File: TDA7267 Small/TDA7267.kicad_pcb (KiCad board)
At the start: 2 copper layers, 43 x 39 mm, 18 parts, among them U1 TDA7267

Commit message: More stuff
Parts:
- D1: footprint LED_THT:LED_D5.0mm -> LED_THT:LED_D3.0mm
- moved OUT1 8.12 mm to (161.7, 88.6)
- moved H1 8.00 mm to (131.8, 89.5)
- moved H2 8.00 mm to (169.2, 89.5)
- moved C6 7.50 mm to (162.9, 96.9)
- moved C2 7.35 mm to (160.5, 106.6)
- moved D1 6.06 mm to (134.2, 94.3)
- moved R2 5.02 mm to (138.1, 89.9)
- moved TDA7267 4.66 mm to (149.6, 94.1)
- moved C5 3.96 mm to (140.9, 94.3)
- moved C3 2.38 mm to (140.6, 105.6)
- moved R1 2.38 mm to (145.6, 107.1)
- moved C1 2.31 mm to (155.5, 105.9)
- moved C4 0.90 mm to (135.5, 101.3)
- moved H3 0.54 mm to (131.8, 108.5)
- moved H4 0.54 mm to (169.2, 108.5)
- renumbered U1 to TDA7267
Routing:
- net Net-(OUT1-Pin_1): track 15.4 -> 11.8 mm
- net Net-(U1-SRV): track 17.7 -> 15.4 mm
- net Net-(C1-Pad1): track 13.1 -> 11.1 mm
- net Net-(U1-Out): track 17.3 -> 18.4 mm
- net Net-(D1-A): track 5.64 -> 4.94 mm
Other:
- board size 43 x 39 mm -> 43 x 31 mm
- board text removed: "TDA7267"

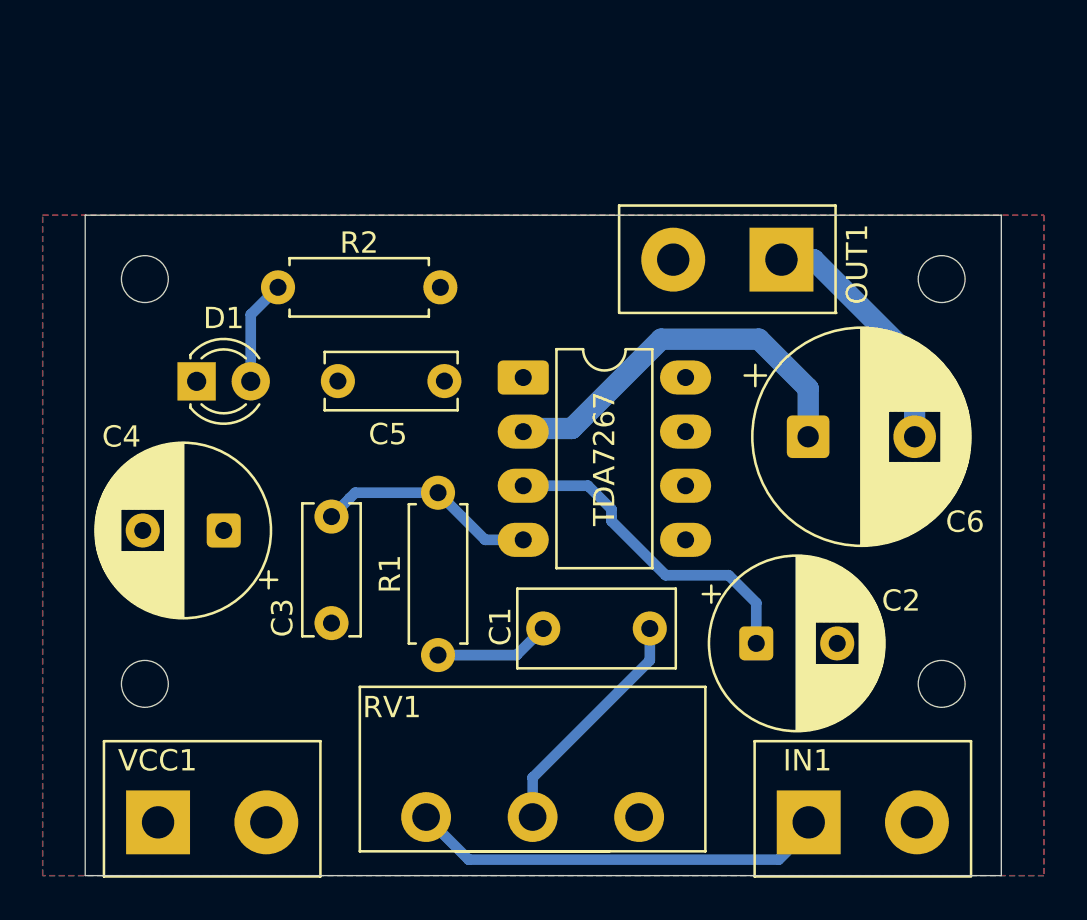
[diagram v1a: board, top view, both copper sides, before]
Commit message: Bottom GND plane
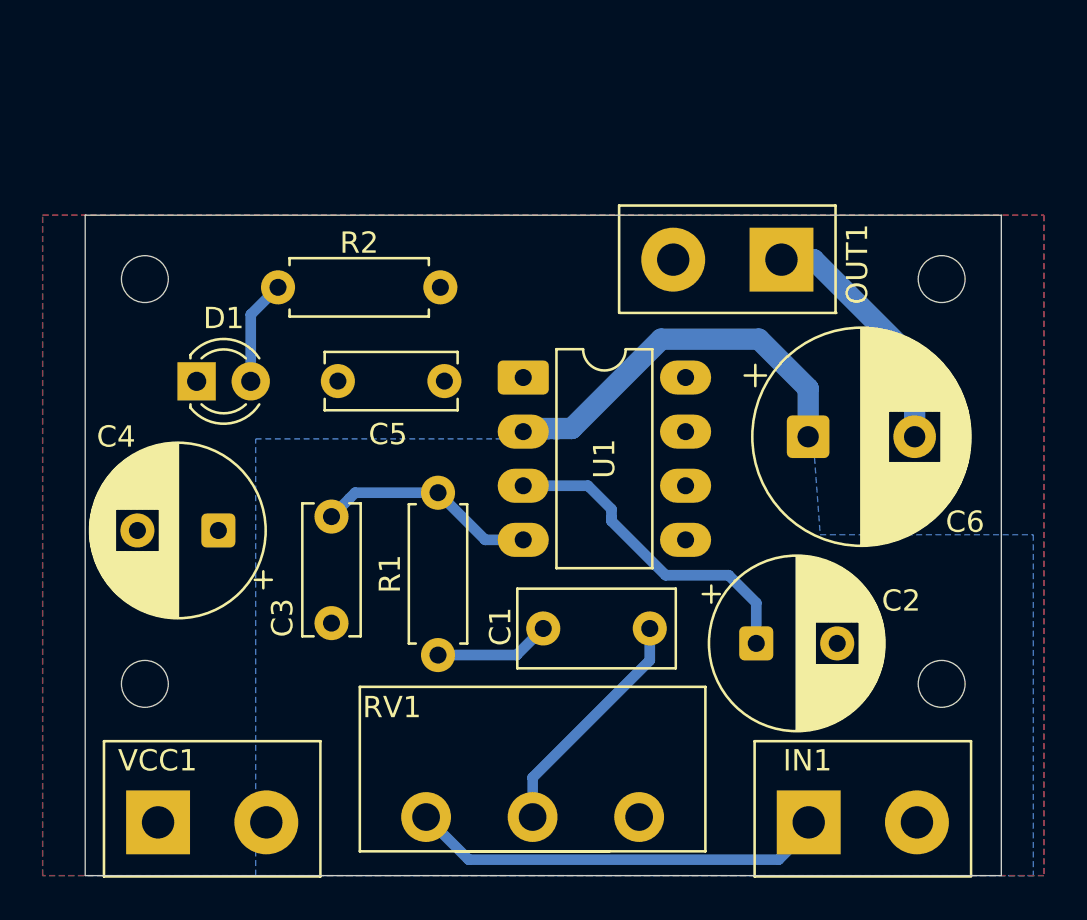
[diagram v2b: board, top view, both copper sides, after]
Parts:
- moved C4 0.25 mm to (135.2, 101.3)
- renumbered TDA7267 to U1
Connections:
- net Net-(U1-V+) renamed /VCC
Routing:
- added copper zone on B.Cu, net GND
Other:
- board text added: "TDA7267 2.5W Amplifier. 5 to 15V DC supply."
- board text removed: "TDA7267 2W Amplifier. 5 to 15V DC supply."
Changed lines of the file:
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@@
 	(net 4 "Net-(U1-SRV)")
 	(net 5 "Net-(U1-In)")
-	(net 6 "Net-(U1-V+)")
+	(net 6 "/VCC")
 	(net 7 "Net-(U1-Out)")
 	(net 8 "Net-(OUT1-Pin_1)")
@@
 			(layers "*.Cu" "*.Mask")
 			(remove_unused_layers no)
-			(net 6 "Net-(U1-V+)")
+			(net 6 "/VCC")
 			(pintype "passive")
 		)
@@
 		(descr "8-lead though-hole mounted DIP package, row spacing 7.62mm (300 mils), LongPads")
 		(tags "THT DIP DIL PDIP 2.54mm 7.62mm 300mil LongPads")
-		(property "Reference" "TDA7267"
+		(property "Reference" "U1"
 			(at 3.81 3.81 90)
 			(layer "F.SilkS")
@@
 			(remove_unused_layers no)
 			(roundrect_rratio 0.15625)
-			(net 6 "Net-(U1-V+)")
+			(net 6 "/VCC")
 			(pinfunction "V+")
 			(pintype "power_in")
@@
 			(layers "*.Cu" "*.Mask")
 			(remove_unused_layers no)
-			(net 6 "Net-(U1-V+)")
+			(net 6 "/VCC")
 			(pintype "passive")
 		)
@@
 			(layers "*.Cu" "*.Mask")
 			(remove_unused_layers no)
-			(net 6 "Net-(U1-V+)")
+			(net 6 "/VCC")
 			(pinfunction "Pin_1")
 			(pintype "passive")
@@
 	(footprint "Capacitor_THT:CP_Radial_D8.0mm_P3.80mm"
 		(layer "F.Cu")
-		(at 135.5 101.3 180)
+		(at 135.25 101.3 180)
 		(descr "CP, Radial series, Radial, pin pitch=3.80mm, diameter=8mm, height=14mm, Electrolytic Capacitor")
 		(tags "CP Radial series Radial pin pitch 3.80mm diameter 8mm height 14mm Electrolytic Capacitor")
@@
 			(remove_unused_layers no)
 			(roundrect_rratio 0.15625)
-			(net 6 "Net-(U1-V+)")
+			(net 6 "/VCC")
 			(pintype "passive")
 		)
@@
 		(layer "Edge.Cuts")
 	)
-	(gr_text "TDA7267 2W Amplifier.\n5 to 15V DC supply."
-		(at 162.4 112.6 0)
+	(gr_text "TDA7267 2.5W Amplifier.\n5 to 15V DC supply."
+		(at 164 112.6 0)
 		(layer "B.SilkS")
 		(effects
@@
 	)
 	(zone
-		(net 6)
-		(net_name "Net-(U1-V+)")
+		(net 3)
+		(net_name "GND")
 		(layer "B.Cu")
 		(hatch edge 0.5)
+		(priority 1)
 		(connect_pads yes
 			(clearance 0.5)
@@
 		(fill yes
 			(thermal_gap 0.5)
-			(thermal_bridge_width 10)
+			(thermal_bridge_width 0.5)
 		)
 		(polygon
 			(pts
-				(xy 127 86.5) (xy 174 86.5) (xy 174 117.5) (xy 127 117.5)
+				(xy 137 117.5) (xy 137 97) (xy 151.25 97) (xy 156.25 92.25) (xy 160.75 92.25) (xy 163 94.75) (xy 163.5 101.5)
+				(xy 173.5 101.5) (xy 173.5 117.5)
 			)
 		)
 	)
 	(zone
-		(net 0)
-		(net_name "")
+		(net 6)
+		(net_name "/VCC")
 		(layer "B.Cu")
 		(hatch edge 0.5)
-		(connect_pads
-			(clearance 0)
+		(connect_pads yes
+			(clearance 0.5)
 		)
 		(min_thickness 0.25)
 		(filled_areas_thickness no)
-		(keepout
-			(tracks allowed)
-			(vias allowed)
-			(pads allowed)
-			(copperpour not_allowed)
-			(footprints allowed)
-		)
-		(placement
-			(enabled no)
-			(sheetname "/")
-		)
-		(fill
+		(fill yes
 			(thermal_gap 0.5)
-			(thermal_bridge_width 0.5)
+			(thermal_bridge_width 10)
 		)
 		(polygon
 			(pts
-				(xy 173.5 117.5) (xy 173.5 101.5) (xy 163.5 101.5) (xy 163.5 97) (xy 136.5 97) (xy 136.5 117.5)
+				(xy 127 86.5) (xy 174 86.5) (xy 174 117.5) (xy 127 117.5)
 			)
 		)
